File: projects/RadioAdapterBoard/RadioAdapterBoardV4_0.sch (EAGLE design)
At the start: 5 parts

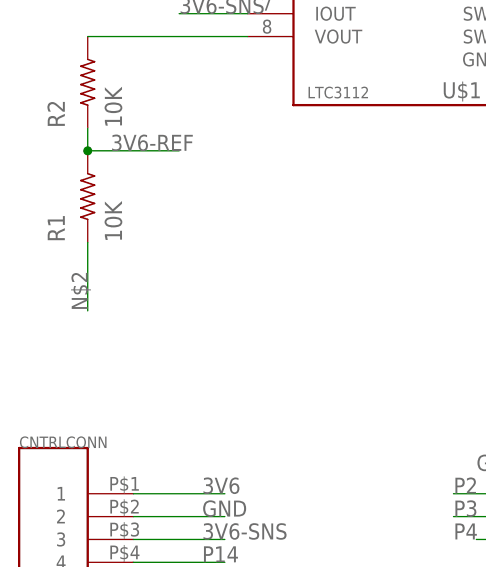
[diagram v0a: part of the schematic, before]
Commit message: Added LTC3112 to Radio Adaptor Board
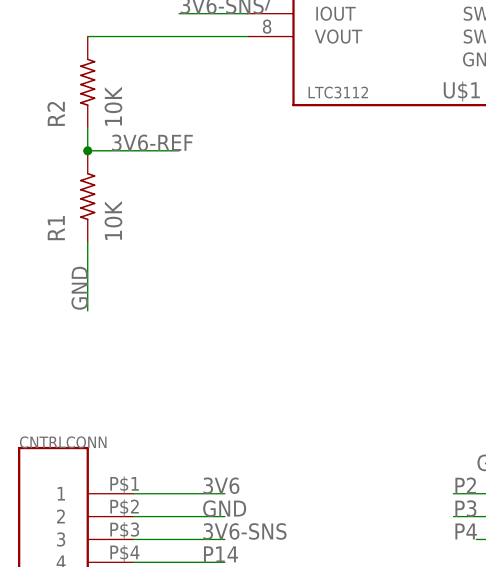
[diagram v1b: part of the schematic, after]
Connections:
- removed net N$2: R1.1
- net GND: now also R1.1
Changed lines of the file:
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@@
 <label x="17.78" y="22.86" size="1.778" layer="95"/>
+</segment>
+<segment>
+<pinref part="R1" gate="R$1" pin="1"/>
+<wire x1="5.08" y1="71.12" x2="5.08" y2="63.5" width="0.1524" layer="91"/>
+<label x="5.08" y="63.5" size="1.778" layer="95" rot="R90"/>
 </segment>
 </net>
@@
 </segment>
 </net>
-<net name="N$2" class="0">
-<segment>
-<pinref part="R1" gate="R$1" pin="1"/>
-<wire x1="5.08" y1="71.12" x2="5.08" y2="63.5" width="0.1524" layer="91"/>
-<label x="5.08" y="63.5" size="1.778" layer="95" rot="R90"/>
-</segment>
-</net>

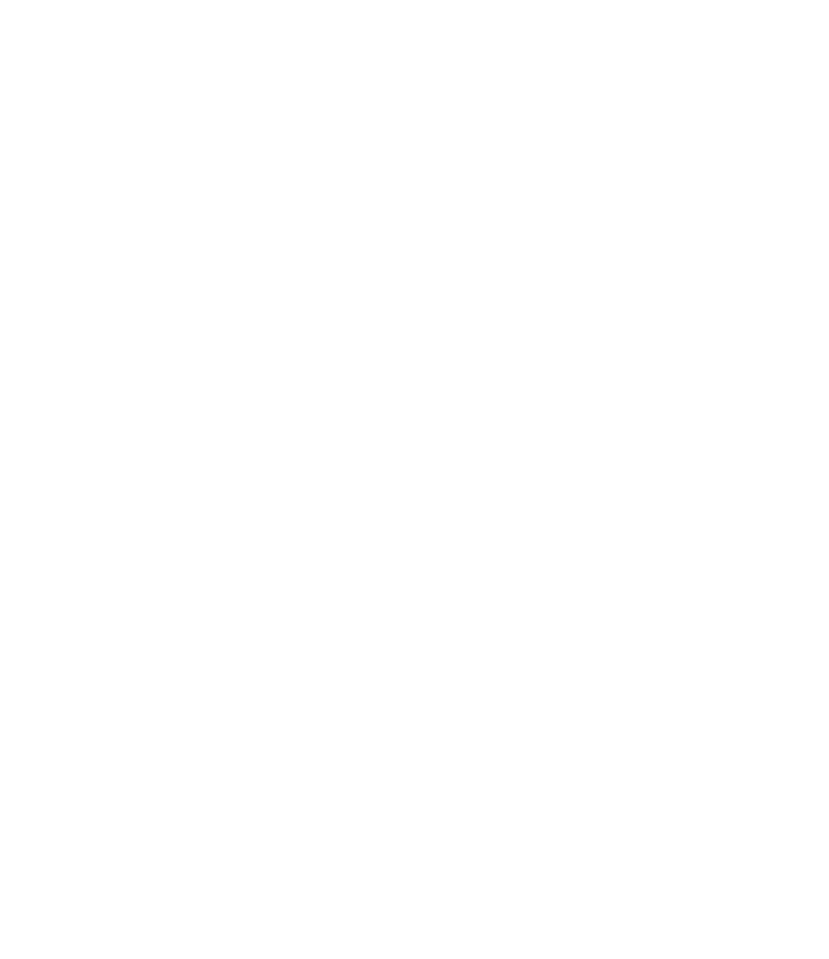
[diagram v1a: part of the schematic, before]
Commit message: Changes to Radio Adapter Board V4
Moved LEDs to Radio Adapter Board
Flipped the connection to the radio so the radio is pointing into the
board
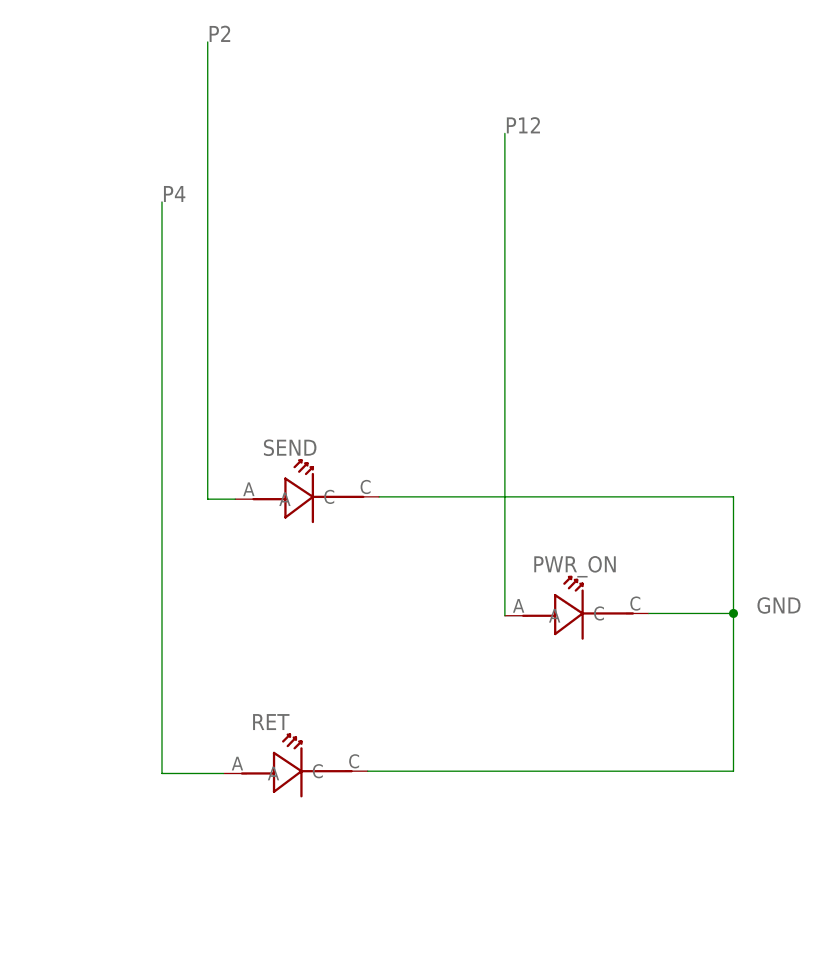
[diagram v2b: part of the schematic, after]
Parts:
- added PWR_ON, RET, SEND: LT-T673-Q1R2-25-Z, CNTRL_BOARD:LT-T673-Q1R2-25-Z
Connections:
- net GND: now also PWR_ON.C, RET.C, SEND.C
- net P12: now also PWR_ON.A
- net P2: now also SEND.A
- net P4: now also RET.A
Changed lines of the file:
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@@
 <class number="0" name="default" width="0" drill="0">
+</class>
+<class number="1" name="GND" width="0.508" drill="0.254">
+<clearance class="1" value="0.3048"/>
 </class>
 </classes>
@@
 <part name="R1" library="BrownSpaceEngineering" deviceset="RES" device="0805" value="10K"/>
 <part name="R2" library="BrownSpaceEngineering" deviceset="RES" device="0805" value="10K"/>
+<part name="PWR_ON" library="CNTRL_BOARD" deviceset="LT-T673-Q1R2-25-Z" device="">
+<attribute name="MF" value=""/>
+<attribute name="MPN" value=""/>
+<attribute name="OC_NEWARK" value="unknown"/>
+</part>
+<part name="RET" library="CNTRL_BOARD" deviceset="LT-T673-Q1R2-25-Z" device="">
+<attribute name="MF" value=""/>
+<attribute name="MPN" value=""/>
+<attribute name="OC_NEWARK" value="unknown"/>
+</part>
+<part name="SEND" library="CNTRL_BOARD" deviceset="LT-T673-Q1R2-25-Z" device="">
+<attribute name="MF" value=""/>
+<attribute name="MPN" value=""/>
+<attribute name="OC_NEWARK" value="unknown"/>
+</part>
 </parts>
 <sheets>
@@
 <instance part="R1" gate="R$1" x="5.08" y="76.2" rot="R90"/>
 <instance part="R2" gate="R$1" x="5.08" y="88.9" rot="R90"/>
+<instance part="PWR_ON" gate="G$1" x="163.068" y="52.832" smashed="yes">
+<attribute name="OC_NEWARK" x="163.068" y="52.832" size="1.778" layer="96" display="off"/>
+<attribute name="MF" x="163.068" y="52.832" size="1.778" layer="96" display="off"/>
+<attribute name="MPN" x="163.068" y="52.832" size="1.778" layer="96" display="off"/>
+<attribute name="NAME" x="160.528" y="57.912" size="1.778" layer="95"/>
+</instance>
+<instance part="RET" gate="G$1" x="131.826" y="35.306" smashed="yes">
+<attribute name="OC_NEWARK" x="131.826" y="35.306" size="1.778" layer="96" display="off"/>
+<attribute name="MF" x="131.826" y="35.306" size="1.778" layer="96" display="off"/>
+<attribute name="MPN" x="131.826" y="35.306" size="1.778" layer="96" display="off"/>
+<attribute name="NAME" x="129.286" y="40.386" size="1.778" layer="95"/>
+</instance>
+<instance part="SEND" gate="G$1" x="133.096" y="65.786" smashed="yes">
+<attribute name="OC_NEWARK" x="133.096" y="65.786" size="1.778" layer="96" display="off"/>
+<attribute name="MF" x="133.096" y="65.786" size="1.778" layer="96" display="off"/>
+<attribute name="MPN" x="133.096" y="65.786" size="1.778" layer="96" display="off"/>
+<attribute name="NAME" x="130.556" y="70.866" size="1.778" layer="95"/>
+</instance>
 </instances>
 <busses>
@@
 <pinref part="AVX" gate="G$1" pin="P$12"/>
 </segment>
+<segment>
+<pinref part="PWR_ON" gate="G$1" pin="A"/>
+<wire x1="157.48" y1="53.086" x2="157.48" y2="106.68" width="0.1524" layer="91"/>
+<label x="157.48" y="106.68" size="1.778" layer="95"/>
+</segment>
 </net>
 <net name="P14" class="0">
@@
 <junction x="55.88" y="43.18"/>
 </segment>
+<segment>
+<pinref part="SEND" gate="G$1" pin="A"/>
+<wire x1="127.508" y1="66.04" x2="124.46" y2="66.04" width="0.1524" layer="91"/>
+<wire x1="124.46" y1="66.04" x2="124.46" y2="116.84" width="0.1524" layer="91"/>
+<label x="124.46" y="116.84" size="1.778" layer="95"/>
+</segment>
 </net>
 <net name="P3" class="0">
@@
 <pinref part="AVX" gate="G$1" pin="P$4"/>
 </segment>
+<segment>
+<pinref part="RET" gate="G$1" pin="A"/>
+<wire x1="126.238" y1="35.56" x2="119.38" y2="35.56" width="0.1524" layer="91"/>
+<wire x1="119.38" y1="35.56" x2="119.38" y2="99.06" width="0.1524" layer="91"/>
+<label x="119.38" y="99.06" size="1.778" layer="95"/>
+</segment>
 </net>
 <net name="GND" class="0">
@@
 <label x="5.08" y="63.5" size="1.778" layer="95" rot="R90"/>
 </segment>
-</net>
+<segment>
+<pinref part="SEND" gate="G$1" pin="C"/>
+<wire x1="143.51" y1="66.294" x2="182.88" y2="66.294" width="0.1524" layer="91"/>
+<wire x1="182.88" y1="66.294" x2="182.88" y2="53.34" width="0.1524" layer="91"/>
+<pinref part="PWR_ON" gate="G$1" pin="C"/>
+<wire x1="182.88" y1="53.34" x2="173.482" y2="53.34" width="0.1524" layer="91"/>
+<pinref part="RET" gate="G$1" pin="C"/>
+<wire x1="142.24" y1="35.814" x2="182.88" y2="35.814" width="0.1524" layer="91"/>
+<wire x1="182.88" y1="35.814" x2="182.88" y2="53.34" width="0.1524" layer="91"/>
+<junction x="182.88" y="53.34"/>
+<label x="185.42" y="53.34" size="1.778" layer="95"/>
+</segment>
+</net>

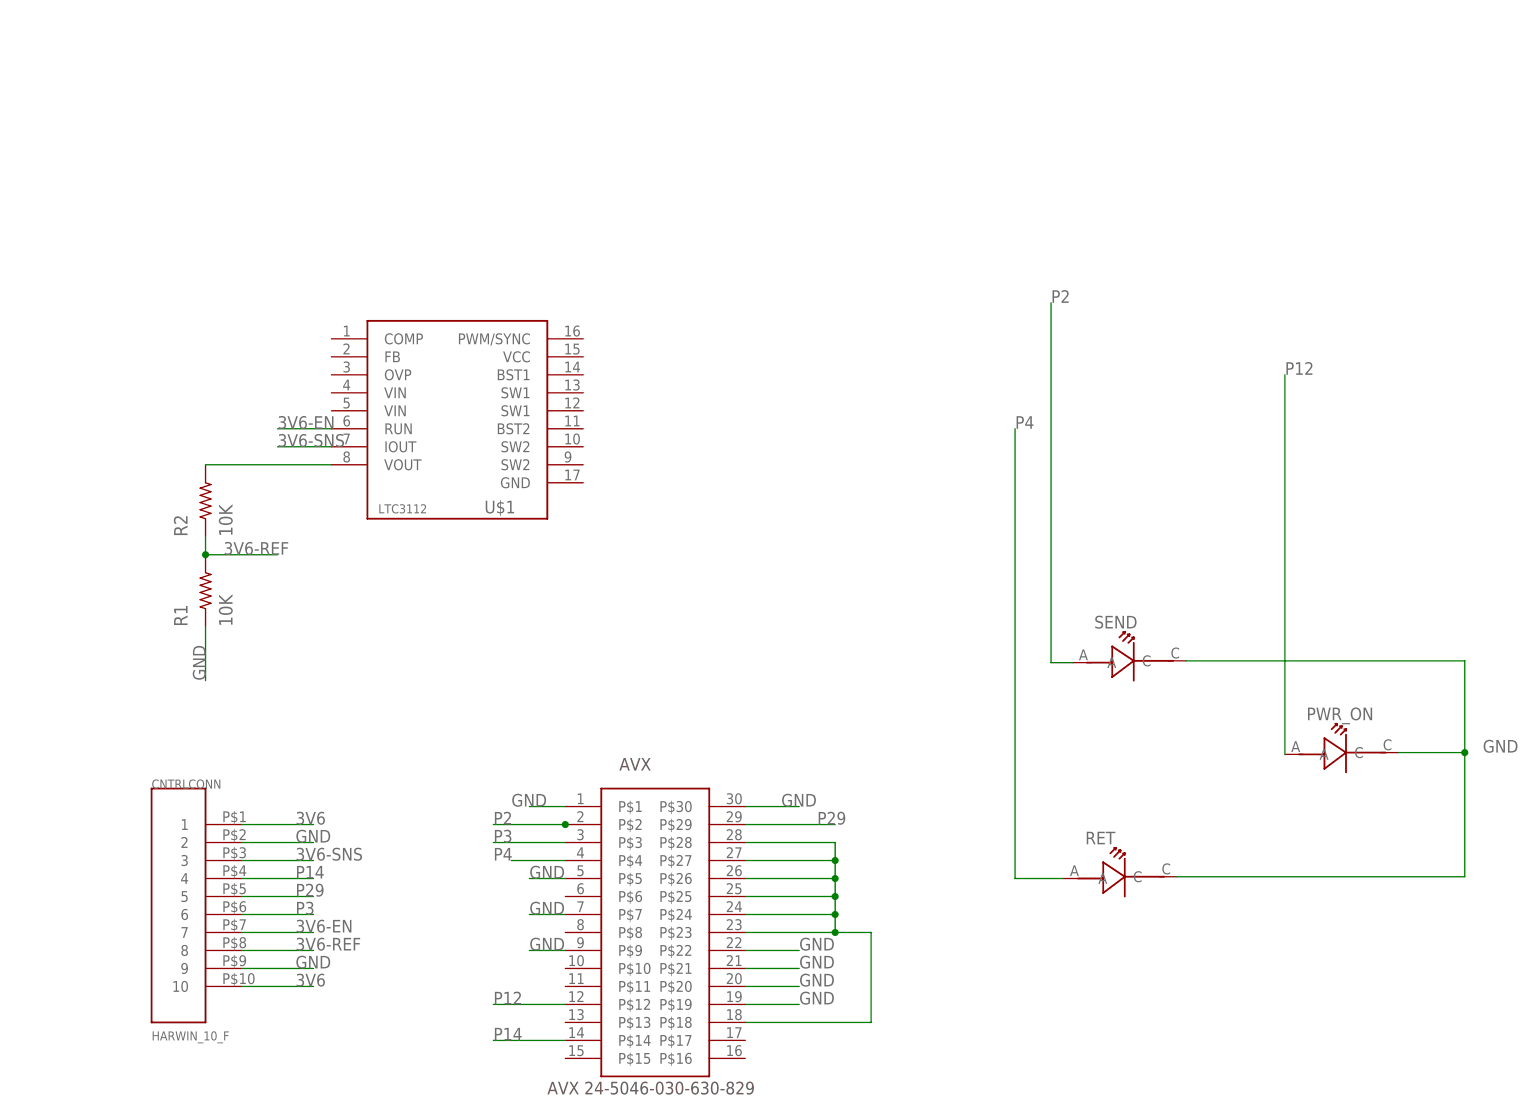
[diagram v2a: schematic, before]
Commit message: changes to Radio Adapter Board V4
Added the connections to LTC3112
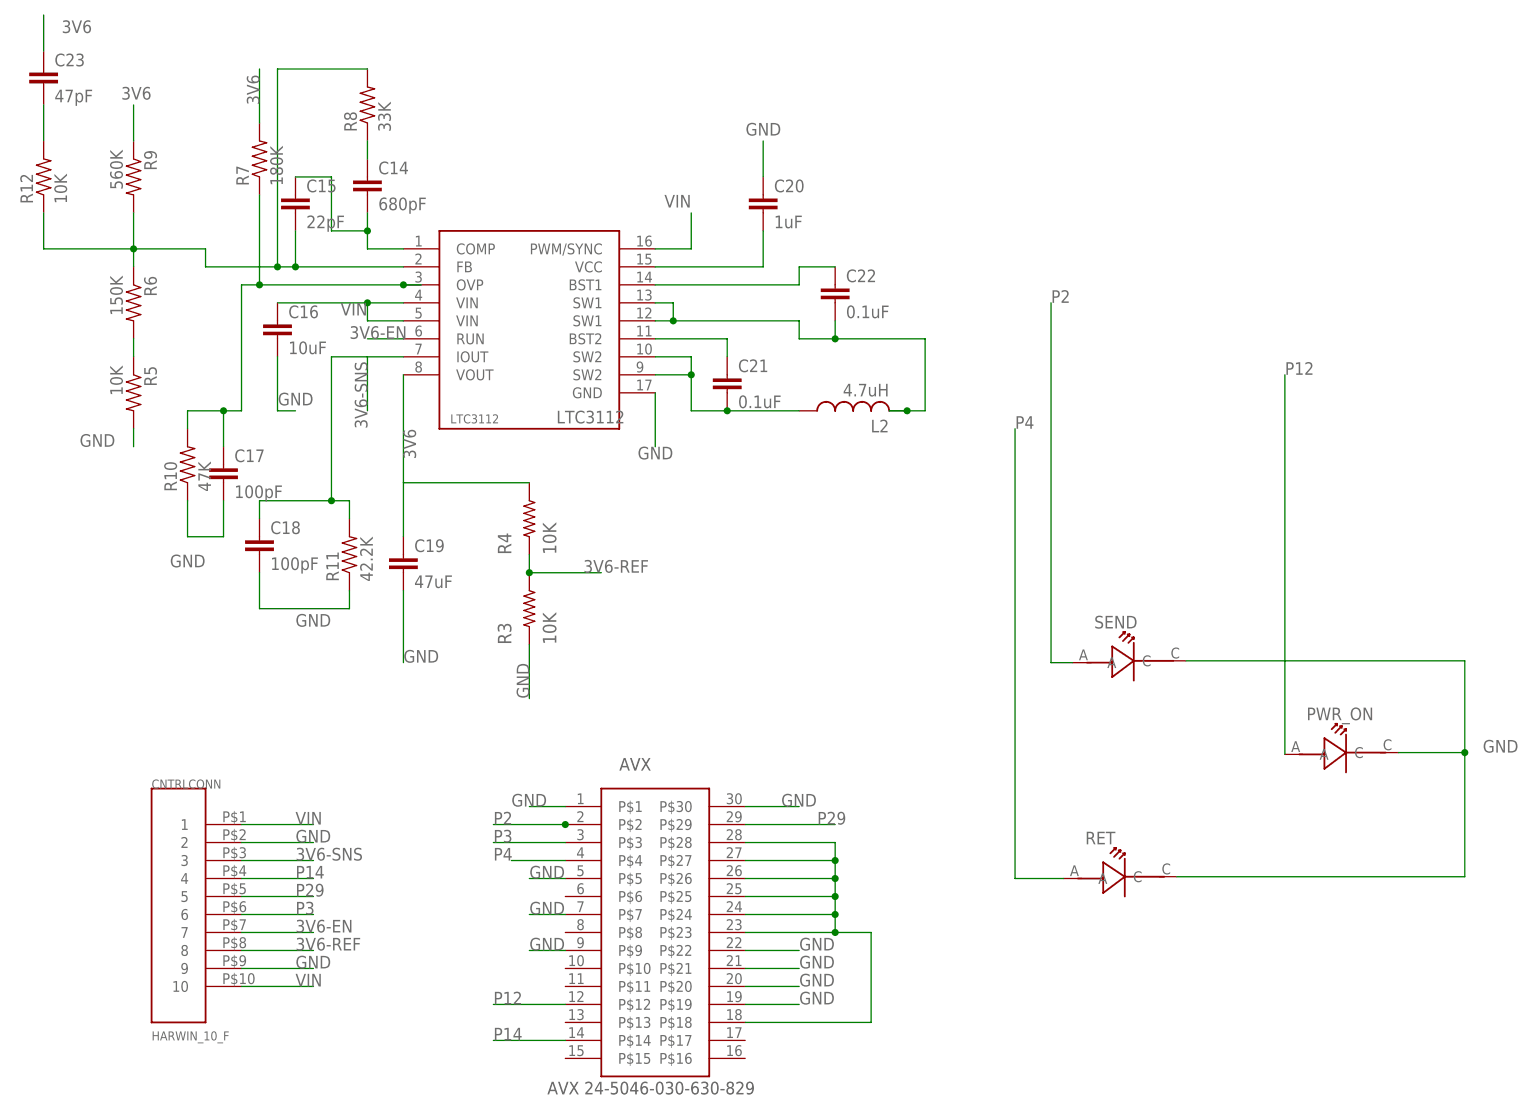
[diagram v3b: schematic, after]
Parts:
- removed R1, R2: 10K, BrownSpaceEngineering:RES0805
- removed U$1: (no value), CNTRL_BOARD:LTC3112
- added C14: 680pF, CNTRL_BOARD:CAP0805
- added C15: 22pF, CNTRL_BOARD:CAP0805
- added C16: 10uF, CNTRL_BOARD:CAP0805
- added C17, C18: 100pF, CNTRL_BOARD:CAP0805
- added C19: 47uF, CNTRL_BOARD:CAP0805
- added C20: 1uF, CNTRL_BOARD:CAP0805
- added C21, C22: 0.1uF, CNTRL_BOARD:CAP0805
- added C23: 47pF, CNTRL_BOARD:CAP0805
- added L2: 4.7uH, resistor:L-USL3225M
- added LTC3112: (no value), CNTRL_BOARD:LTC3112
- added R10: 47K, CNTRL_BOARD:RESISTOR
- added R11: 42.2K, CNTRL_BOARD:RESISTOR
- added R12, R5: 10K, CNTRL_BOARD:RESISTOR
- added R3, R4: 10K, BrownSpaceEngineering:RES0805
- added R6: 150K, CNTRL_BOARD:RESISTOR
- added R7: 180K, CNTRL_BOARD:RESISTOR
- added R8: 33K, CNTRL_BOARD:RESISTOR
- added R9: 560K, CNTRL_BOARD:RESISTOR
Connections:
- removed net N$3: R2.2, U$1.VOUT
- new net COMP: C14.2, C15.1, LTC3112.COMP
- new net FB: C15.2, LTC3112.FB, R12.1, R6.1, R8.2, R9.2
- new net N$23: C20.2, LTC3112.VCC
- new net N$25: C22.1, LTC3112.BST1
- new net N$26: C22.2, L2.2, LTC3112.SW1@1, LTC3112.SW1@2
- new net N$28: C21.2, L2.1, LTC3112.SW2@1, LTC3112.SW2@2
- new net N$29: C21.1, LTC3112.BST2
- new net N$4: C14.1, R8.1
- new net N$5: C23.2, R12.2
- new net N$6: R5.1, R6.2
- new net OVP: C17.1, LTC3112.OVP, R10.2, R7.1
- new net VIN: C16.1, CNTRLCONN.1, CNTRLCONN.10, LTC3112.PWM/SYNC, LTC3112.VIN@1, LTC3112.VIN@2
- net 3V6: now also C19.1, C23.1, LTC3112.VOUT, R4.2, R7.2, R9.1; no longer CNTRLCONN.1, CNTRLCONN.10
- net 3V6-EN: now also LTC3112.RUN; no longer U$1.RUN
- net 3V6-REF: now also R3.2, R4.1; no longer R1.2, R2.1
- net 3V6-SNS: now also C18.1, LTC3112.IOUT, R11.2; no longer U$1.IOUT
- net GND: now also C16.2, C17.2, C18.2, C19.2, C20.1, LTC3112.GND, R10.1, R11.1, R3.1, R5.2; no longer R1.1

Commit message: Updates to the Radio Adapter Board
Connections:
- net P12: no longer PWR_ON.A
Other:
- moved on the sheet: C14, C15, C16, C17, C18, C19, C20, C21, C22, C23, L2, LTC3112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
